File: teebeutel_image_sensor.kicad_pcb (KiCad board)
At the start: 2 copper layers, 60 x 27 mm, 42 parts, among them J1 Conn, J2 Conn, Q1 AO3400, Q2 AO3400, U1 OV6946, U2 OVM6948, U3 AMG8834, U4 VL53L5CX, X1 ASE-xxxMHz

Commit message: added gerber
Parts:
- added G***: LOGO, otter:ears_6125, B.Cu at (100.0, 86.7)
- added G***: LOGO, otter:whisker_5322, F.Cu at (100.0, 90.0)
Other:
- outline, holes or cut-outs redrawn
- board text added: "design by @_Jana_Marie 2021-12"
- board text added: "github.com/Jana-Marie/Teebeutel-Image-Sensor-Expansion"
- board text removed: "by Jana Marie @_Jana_Marie 2021-12"

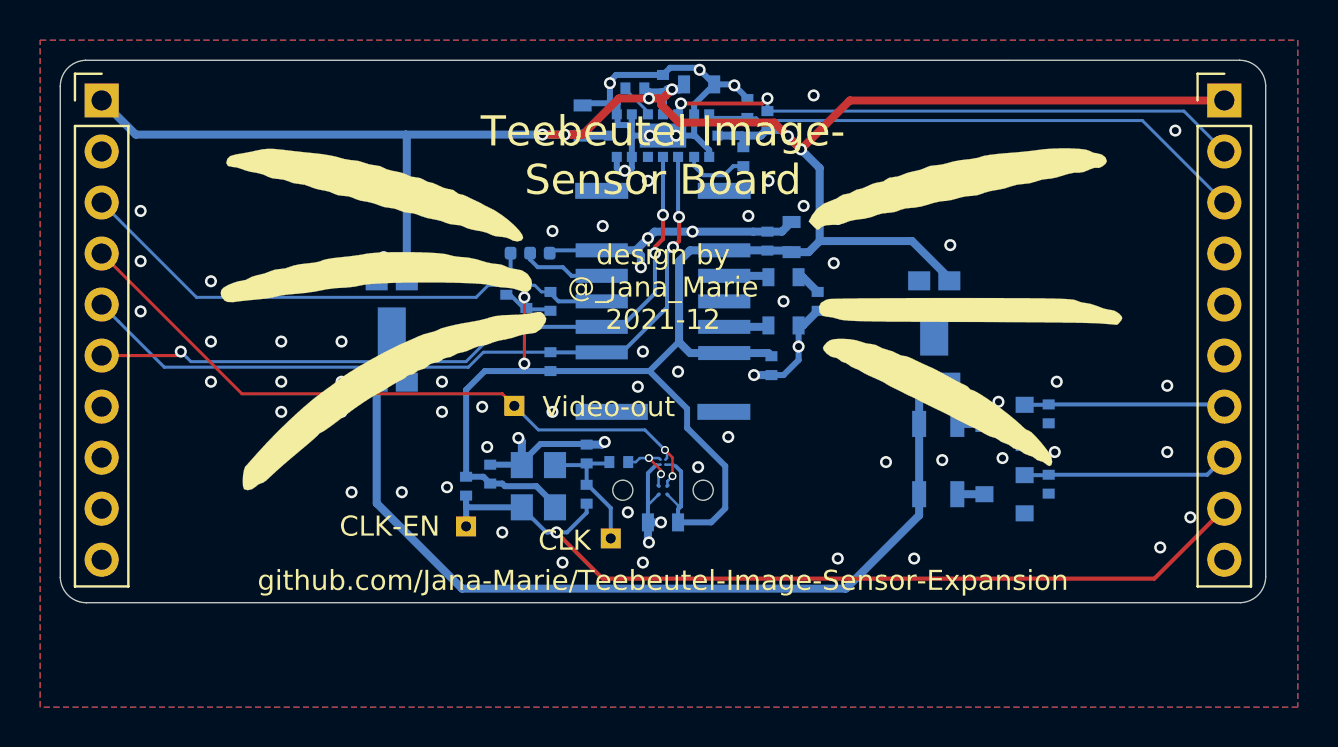
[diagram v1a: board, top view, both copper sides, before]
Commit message: moved to kicad 6, generated gerber
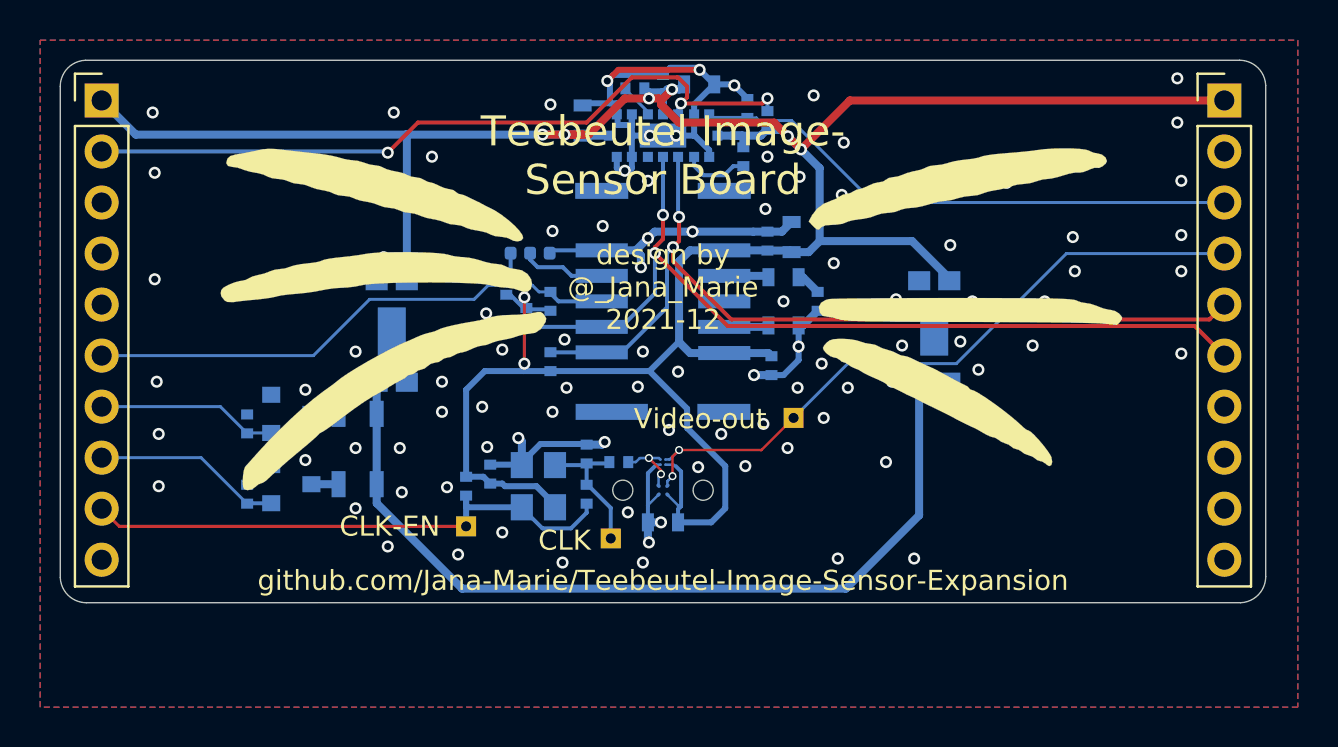
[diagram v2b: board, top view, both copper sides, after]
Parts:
- moved J1 55.9 mm to (127.9, 80.0)
- moved J2 55.9 mm to (72.1, 80.0)
- moved R14 39.9 mm to (79.3, 96.1), turned to 90 degrees
- moved R8 39.9 mm to (79.3, 99.6), turned to 90 degrees
- moved Q1 35.5 mm to (81.5, 99.1), turned to 0 degrees
- moved Q2 35.5 mm to (81.5, 95.6), turned to 0 degrees
- moved R15 28.9 mm to (84.8, 99.1), turned to 180 degrees
- moved R16 28.9 mm to (84.8, 95.6), turned to 180 degrees
- moved TP2 13.9 mm to (106.5, 95.8)
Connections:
- R10 pad 2: IO1 -> IO8
- R11 pad 2: IO8 -> IO4
- U3 pad 1: Net-(U3-Pad1) -> unconnected-(U3-Pad1)
- U3 pad 11: Net-(U3-Pad11) -> unconnected-(U3-Pad11)
- U3 pad 14: Net-(U3-Pad14) -> unconnected-(U3-Pad14)
- U3 pad 4: IO8 -> IO4
- U3 pad 7: Net-(U3-Pad7) -> unconnected-(U3-Pad7)
- U3 pad 8: Net-(U3-Pad8) -> unconnected-(U3-Pad8)
- U4 pad A1: IO1 -> IO8
- U4 pad C5: Net-(U4-PadC5) -> unconnected-(U4-PadC5)
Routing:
- net IO1: track 27.5 -> 0.00 mm
- net IO4: track 0.00 -> 26.9 mm
- net IO7: track 45.1 -> 27.8 mm, vias 1 -> 0
- net IO0: track 29.2 -> 37.5 mm, vias 2 -> 3
- net SCL: track 36.4 -> 44.5 mm, vias 3 -> 2
- net SDA: track 38.4 -> 44.1 mm
- net GND: track 57.8 -> 62.8 mm, vias 72 -> 95
- net IO5: track 9.99 -> 9.00 mm
- net IO6: track 10.3 -> 9.37 mm
- net IO9: track 34.7 -> 34.1 mm
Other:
- net class Default removed
